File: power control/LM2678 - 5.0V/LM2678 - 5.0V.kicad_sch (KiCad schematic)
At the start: 14 parts, among them J1 Conn_01x04_Pin, J2 Conn_01x04_Pin, J3 Conn_01x03_Pin, U1 TPS79633KTTR, U2 LM2678S-12

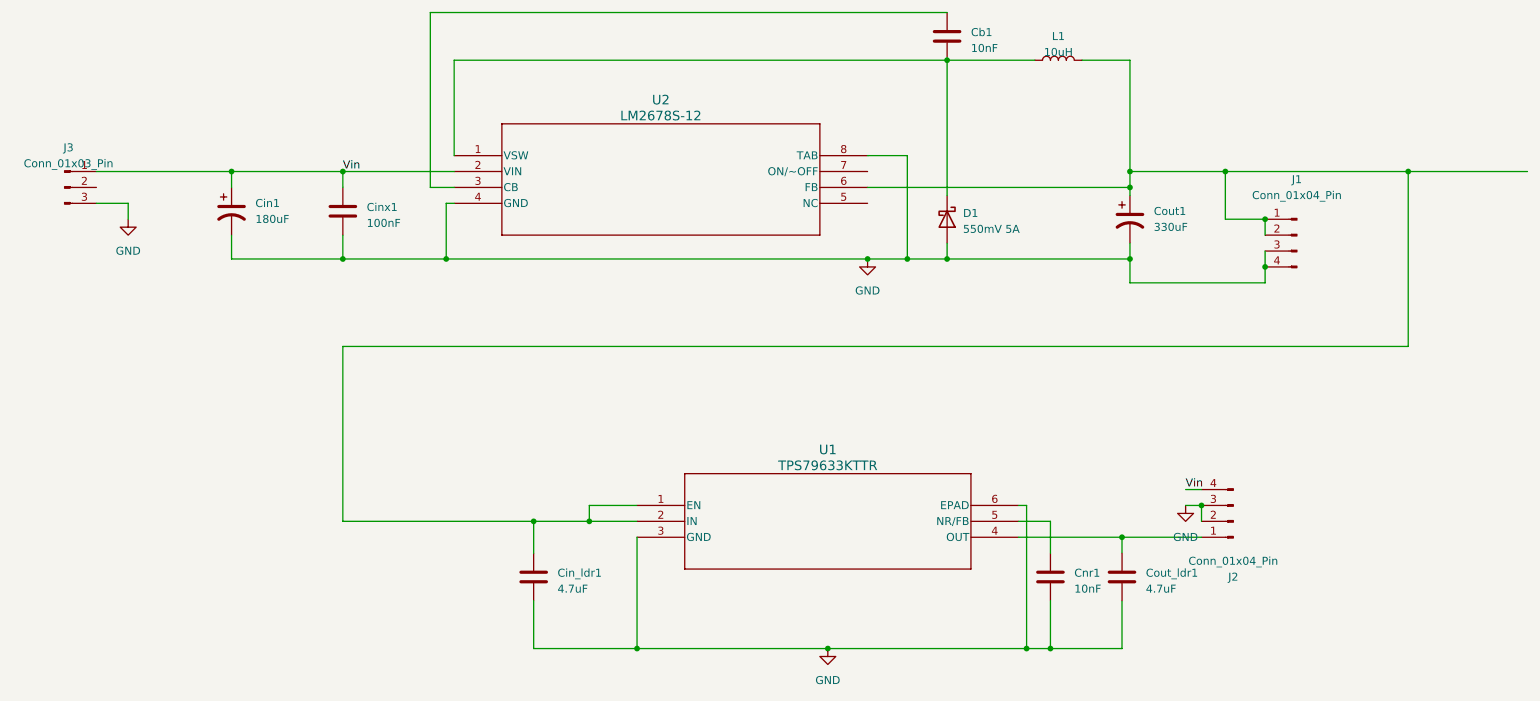
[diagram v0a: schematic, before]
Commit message: fixed power circuit
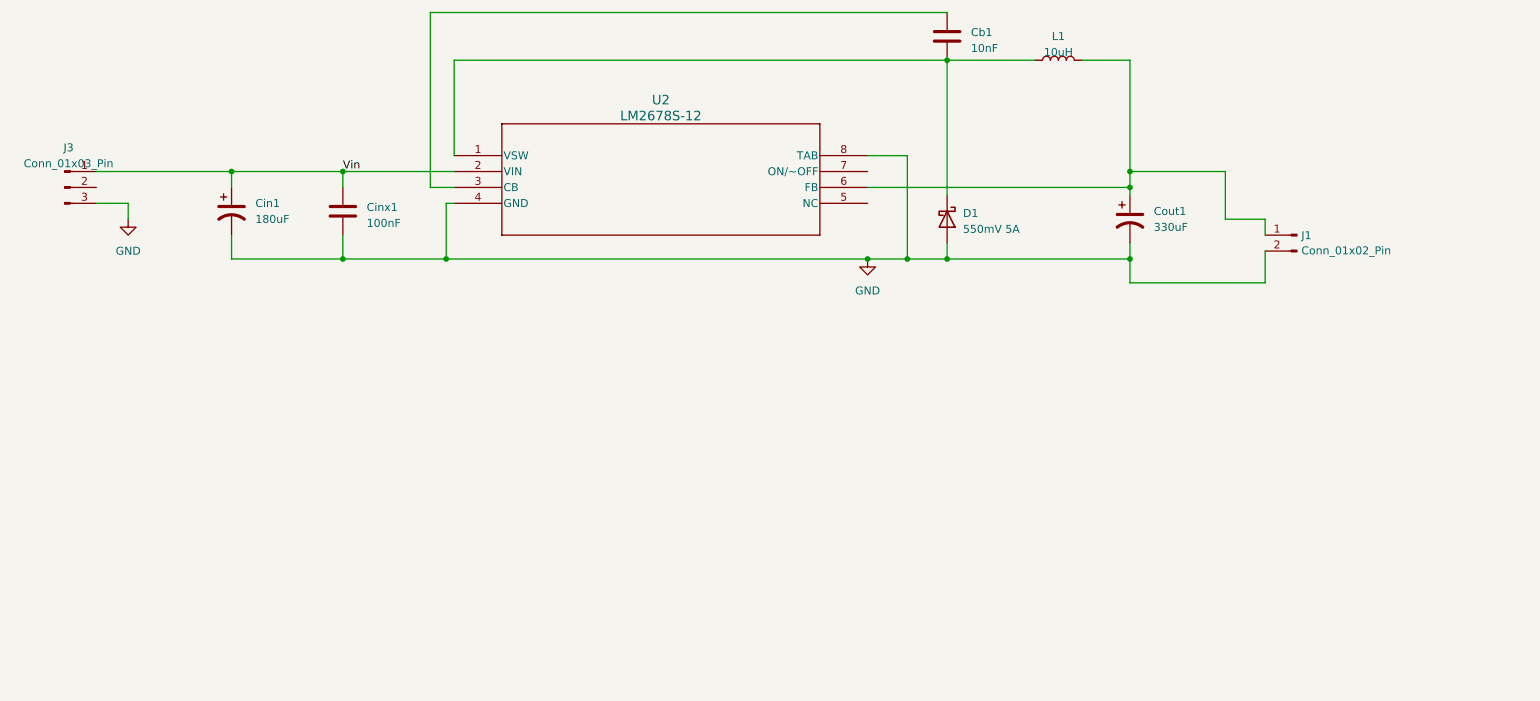
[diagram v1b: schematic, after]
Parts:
- removed Cin_ldr1, Cout_ldr1: 4.7uF, Capacitor_SMD:C_0805_2012Metric_Pad1.18x1.45mm_HandSolder, symbol Device:C
- removed Cnr1: 10nF, Capacitor_SMD:C_0805_2012Metric_Pad1.18x1.45mm_HandSolder, symbol Device:C
- removed J1, J2: Conn_01x04_Pin, Connector_JST:JST_VH_B4P-VH-B_1x04_P3.96mm_Vertical, symbol Connector:Conn_01x04_Pin
- removed U1: TPS79633KTTR, TPS79633KTTR:KTT5_6P22X6P86_TEX, symbol TPS79633:TPS79633KTTR
- added J1: Conn_01x02_Pin, Connector_PinHeader_2.54mm:PinHeader_1x02_P2.54mm_Vertical, symbol Connector:Conn_01x02_Pin
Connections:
- net GND: now also J1.2 (Pin_2)
- net at Cout1.1, L1.2, U2.6 (FB): now also J1.1 (Pin_1)
